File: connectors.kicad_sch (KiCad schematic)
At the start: 1 part, among them J1 Header_to_RPi

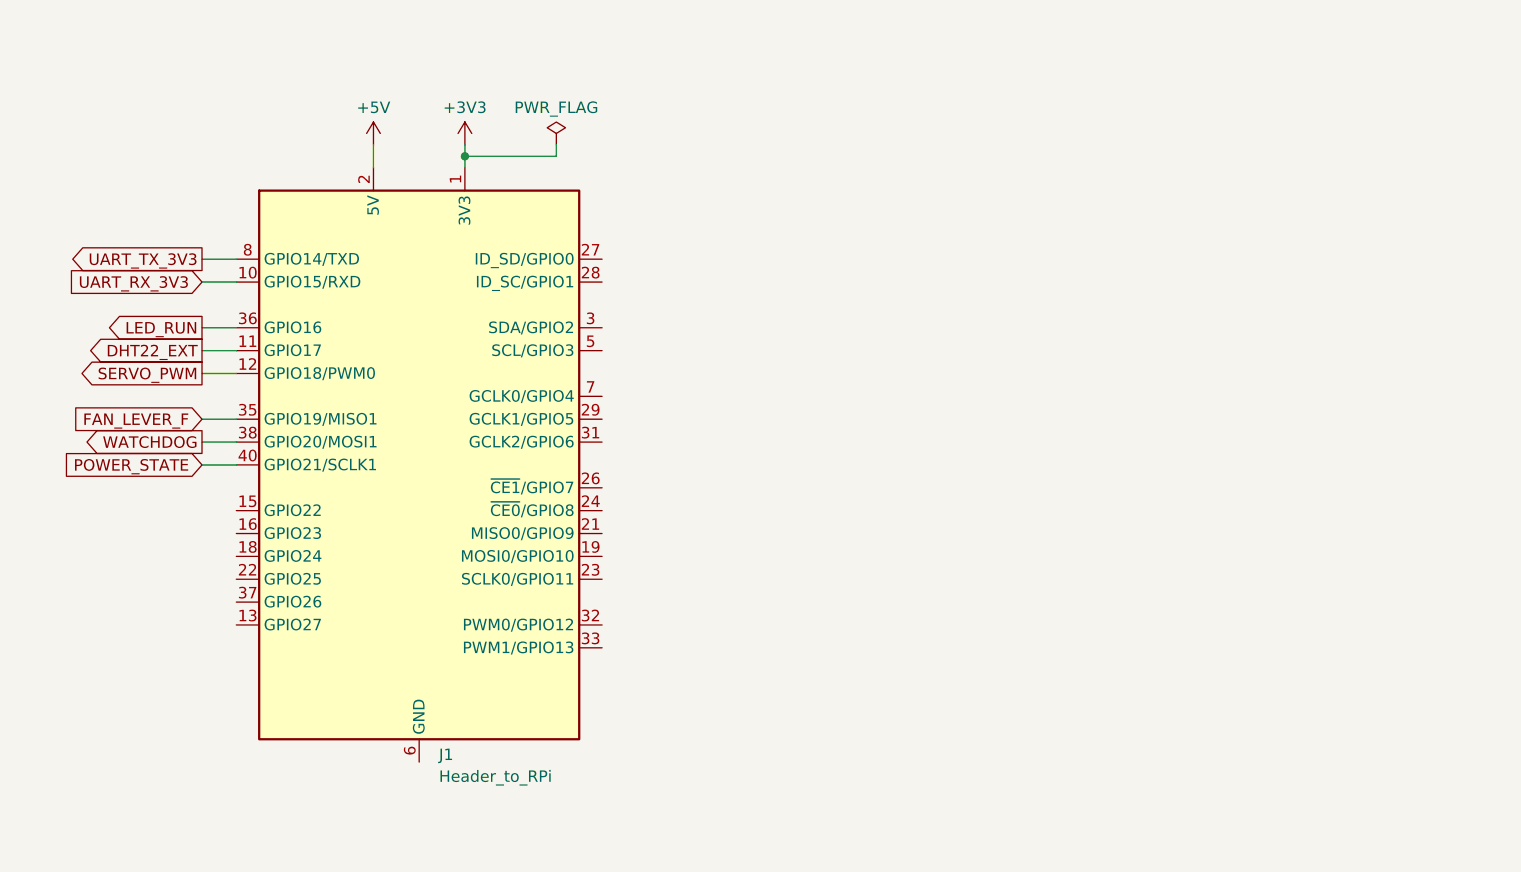
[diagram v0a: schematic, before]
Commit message: Connectors for RPi and front panel done (sch)
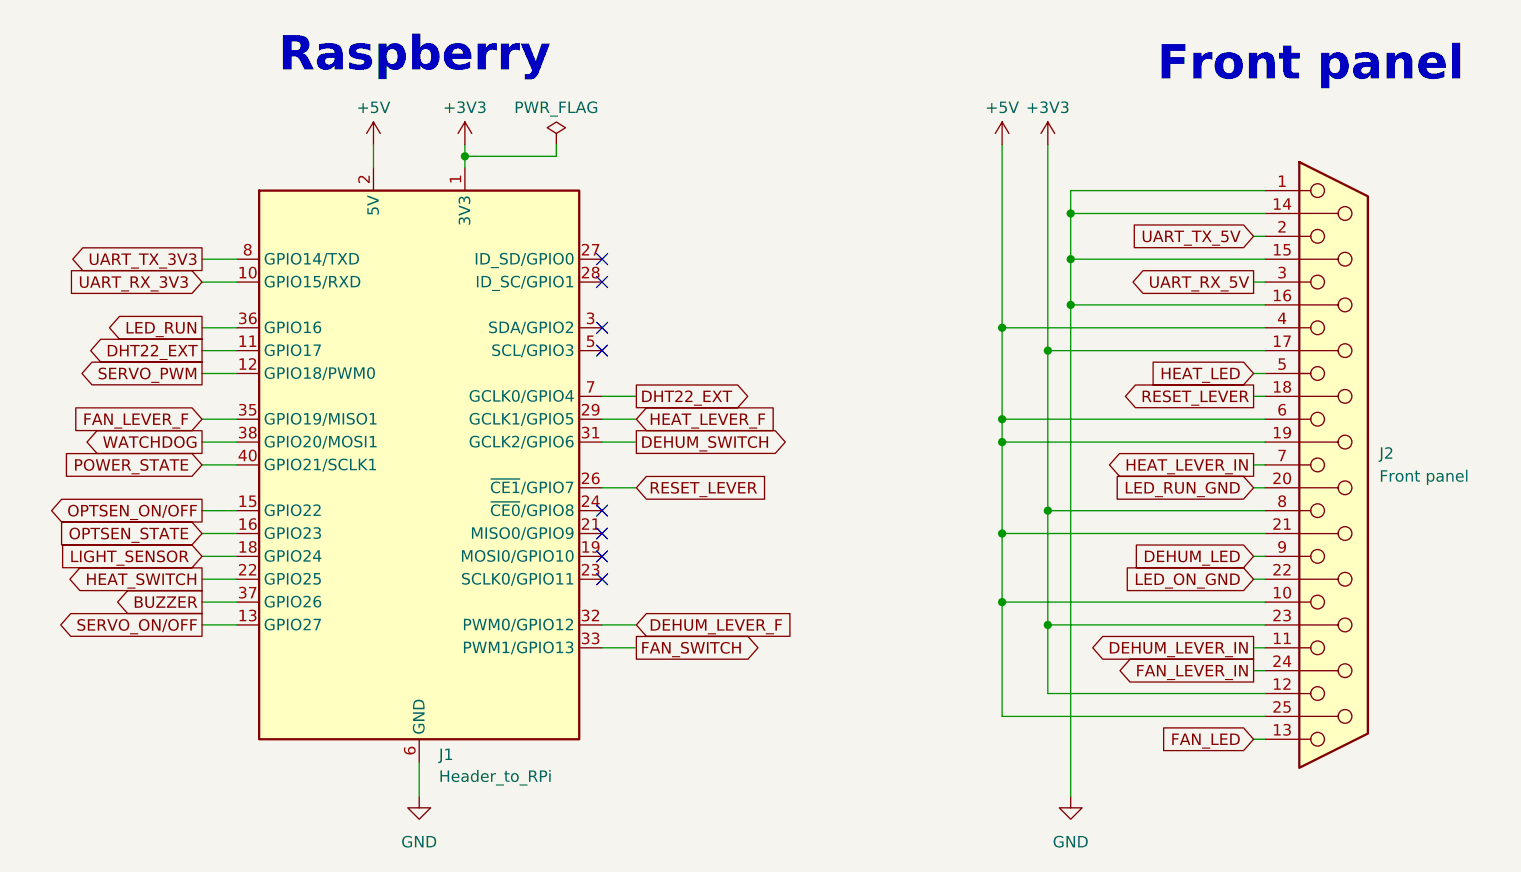
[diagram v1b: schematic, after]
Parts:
- added J2: Front panel, symbol Connector:DB25_Receptacle
- J1: footprint (none) -> Connector_PinHeader_2.54mm:PinHeader_2x20_P2.54mm_Vertical
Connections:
- net +3V3: now also J2.12, J2.17 (P17), J2.23 (P23), J2.8
- net +5V: now also J2.10, J2.19 (P19), J2.21 (P21), J2.25 (P25), J2.4, J2.6
- net DHT22_EXT: now also J1.7 (GCLK0/GPIO4)
- net SERVO_ON/OFF: now reaches J1.13 (GPIO27)
- net GND: now reaches J1.14 (GND), J1.20 (GND), J1.25 (GND), J1.30 (GND), J1.34 (GND), J1.39 (GND), J1.6 (GND), J1.9 (GND)
- net GND: now also J2.1, J2.14 (P14), J2.15 (P15), J2.16 (P16)
- net OPTSEN_ON/OFF: now reaches J1.15 (GPIO22)
- net OPTSEN_STATE: now reaches J1.16 (GPIO23)
- net LIGHT_SENSOR: now reaches J1.18 (GPIO24)
- net HEAT_SWITCH: now reaches J1.22 (GPIO25)
- net RESET_LEVER: now reaches J1.26 (~{CE1}/GPIO7)
- net RESET_LEVER: now also J2.18 (P18)
- net HEAT_LEVER_F: now reaches J1.29 (GCLK1/GPIO5)
- net DEHUM_SWITCH: now reaches J1.31 (GCLK2/GPIO6)
- net DEHUM_LEVER_F: now reaches J1.32 (PWM0/GPIO12)
- net FAN_SWITCH: now reaches J1.33 (PWM1/GPIO13)
- net BUZZER: now reaches J1.37 (GPIO26)
- new net DEHUM_LED: J2.9
- new net DEHUM_LEVER_IN: J2.11
- new net FAN_LED: J2.13
- new net FAN_LEVER_IN: J2.24 (P24)
- new net HEAT_LED: J2.5
- new net HEAT_LEVER_IN: J2.7
- new net LED_ON_GND: J2.22 (P22)
- new net LED_RUN_GND: J2.20 (P20)
- new net UART_RX_5V: J2.3
- new net UART_TX_5V: J2.2
- no-connect marks 0 -> 8
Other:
- note added: "Front panel"
- note added: "Raspberry"

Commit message: Connectors done, WIP on power
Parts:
- added J10: DHT INT, symbol Connector:Conn_01x03_Pin
- added J11: DHT EXT, symbol Connector:Conn_01x03_Pin
- added J3: DEHUM, symbol Connector:Conn_01x02_Pin
- added J4: HEAT, symbol Connector:Conn_01x02_Pin
- added J5: FAN, symbol Connector:Conn_01x02_Pin
- added J6: BUZZER, symbol Connector:Conn_01x02_Pin
- added J7: LIGHTSENSOR, symbol Connector:Conn_01x02_Pin
- added J8: SERVO, symbol Connector:Conn_01x03_Pin
- added J9: POWER_IN, symbol Connector:Conn_01x02_Pin
- added R1, R2: 4.7k, symbol Device:R
- J2: footprint (none) -> Connector_Dsub:DSUB-25_Female_Vertical_P2.77x2.84mm
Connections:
- net +3V3: now also J10.3 (Pin_3), J11.3 (Pin_3), J7.1 (Pin_1), R1.2, R2.2
- net +5V: now also J8.3 (Pin_3)
- net DHT22_EXT: now also J11.2 (Pin_2), R2.1
- net GND: now also J10.1 (Pin_1), J11.1 (Pin_1), J9.1 (Pin_1)
- net SERVO_PWM: now also J8.2 (Pin_2)
- new net +12V: J6.2 (Pin_2)
- new net BUZZER_GND: J6.1 (Pin_1)
- new net DEHUM_RELAY_+: J3.2 (Pin_2)
- new net DEHUM_RELAY_GND: J3.1 (Pin_1)
- new net DHT22_INT: J10.2 (Pin_2), R1.1
- new net FAN_RELAY_+: J5.2 (Pin_2)
- new net FAN_RELAY_GND: J5.1 (Pin_1)
- new net HEAT_RELAY_+: J4.2 (Pin_2)
- new net HEAT_RELAY_GND: J4.1 (Pin_1)
- new net LIGHTSEN_SIG: J7.2 (Pin_2)
- new net POWER+: J9.2 (Pin_2)
- new net SERVO_GND: J8.1 (Pin_1)
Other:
- note added: "Buzzer"
- note added: "DHT EXT"
- note added: "DHT INT"
- note added: "Dehum"
- note added: "Fan"
- note added: "Heat"
- note added: "Light sensor"
- note added: "Power IN"
- note added: "Servo"

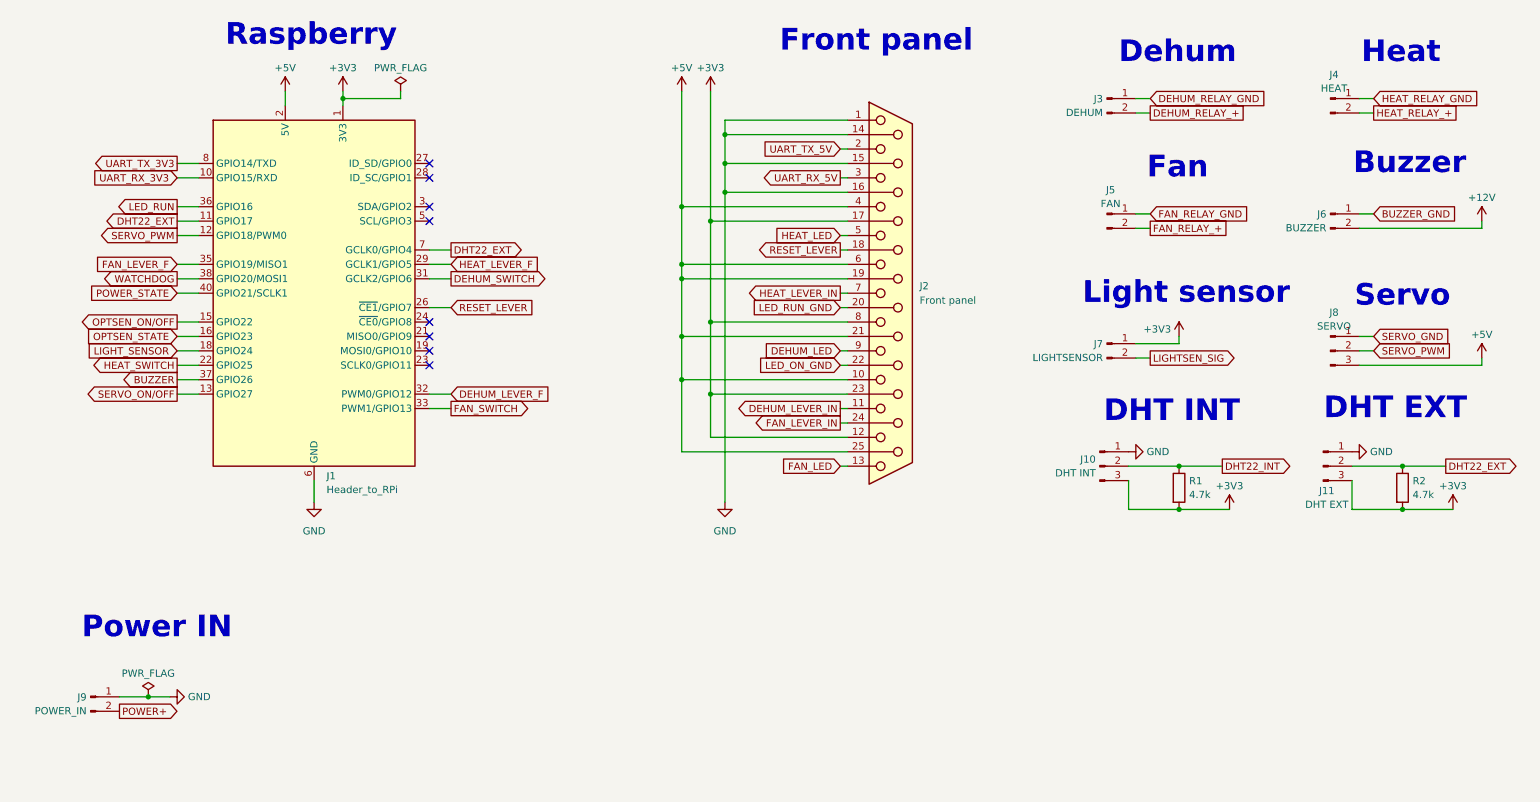
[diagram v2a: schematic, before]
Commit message: Added power surge protection
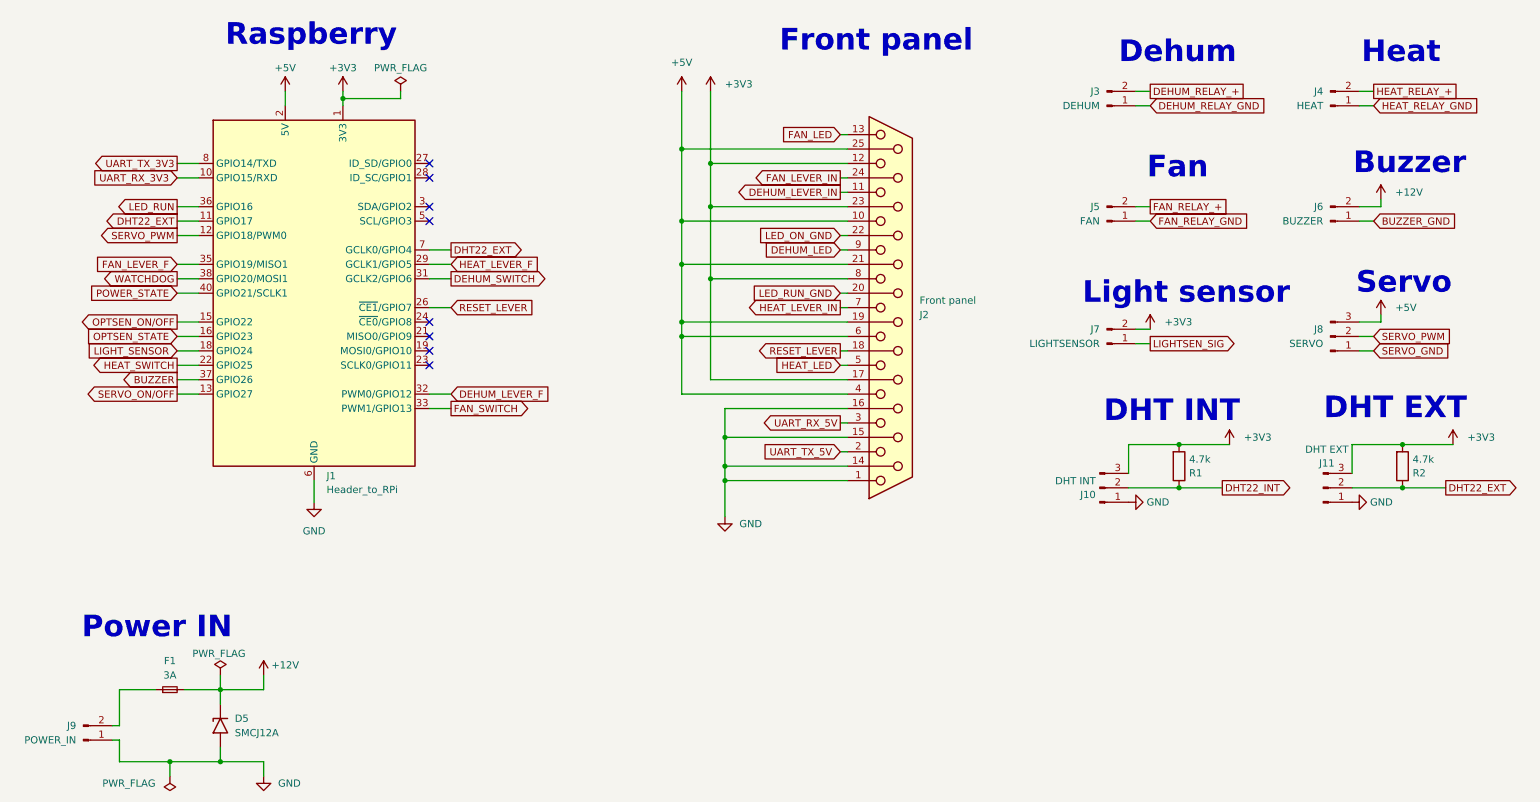
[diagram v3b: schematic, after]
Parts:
- added D5: SMCJ12A, Diode_SMD:D_SMA, symbol Diode:SMAJ12A
- added F1: 3A, symbol Device:Fuse_Small
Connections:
- net +12V: now also D5.1 (A1), F1.2
- net +3V3: now also J7.2 (Pin_2); no longer J7.1 (Pin_1)
- net GND: now also D5.2 (A2)
- net LIGHTSEN_SIG: now also J7.1 (Pin_1); no longer J7.2 (Pin_2)
- net POWER+: no longer names the net of J9.2 (Pin_2)
- net POWER+: now also F1.1
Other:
- moved on the sheet: J10, J11, J2, J3, J4, J5, J6, J7, J8, J9, R1, R2

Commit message: Schematic done (for now), WIP on layout
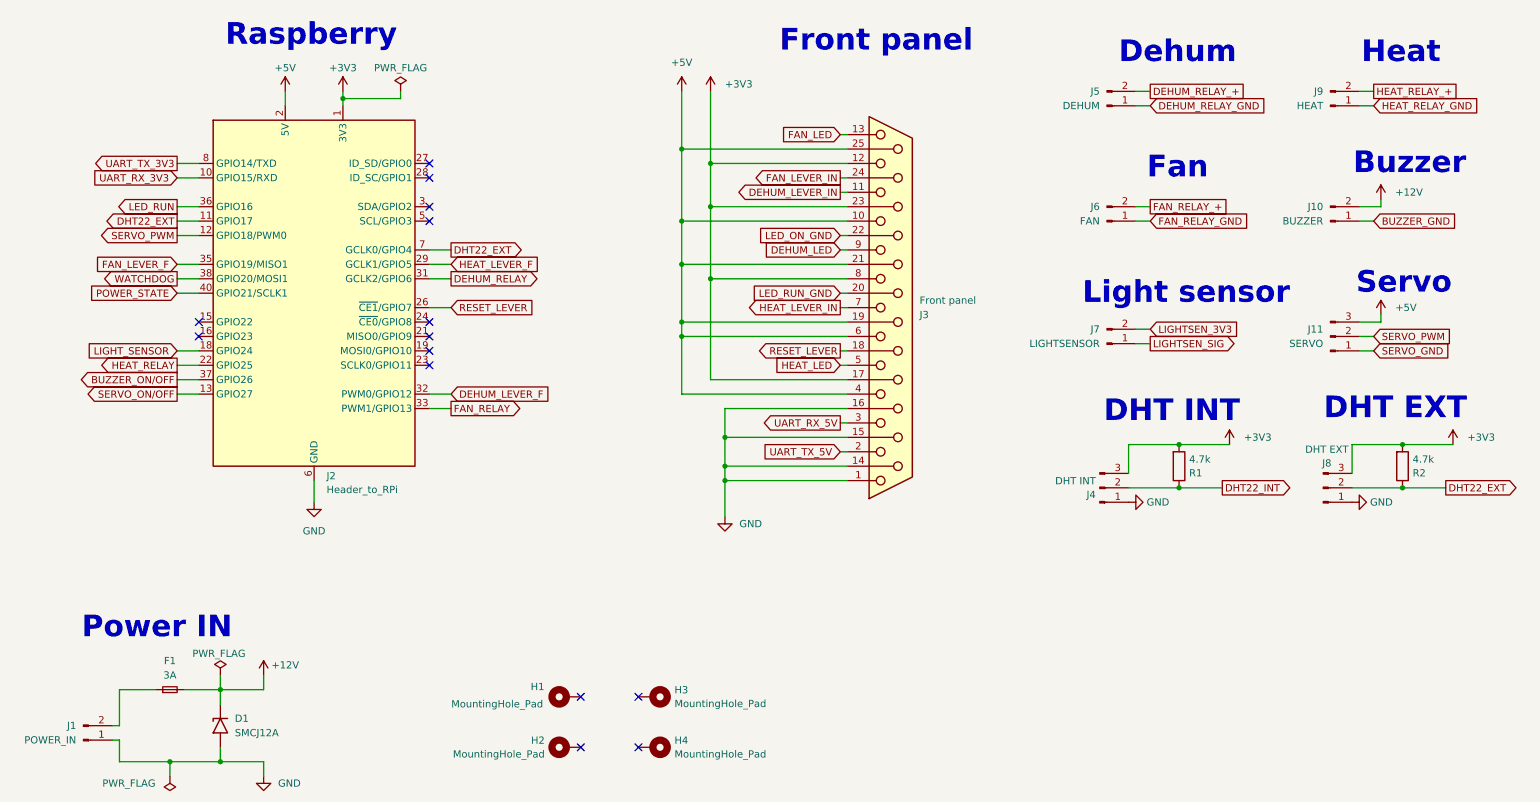
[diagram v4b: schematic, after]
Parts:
- added H1, H2, H3, H4: MountingHole_Pad, MountingHole:MountingHole_2.2mm_M2_ISO14580_Pad_TopBottom, symbol Mechanical:MountingHole_Pad
- D1: renamed from D5; footprint Diode_SMD:D_SMA -> Diode_SMD:D_SMC_Handsoldering
- F1: footprint (none) -> Fuse:Fuseholder_Littelfuse_Nano2_154x
- J1: renamed from J9; footprint (none) -> Connector_JST:JST_XH_B2B-XH-A_1x02_P2.50mm_Vertical
- J10: renamed from J6; footprint (none) -> Connector_JST:JST_XH_B2B-XH-A_1x02_P2.50mm_Vertical
- J11: renamed from J8; footprint (none) -> Connector_JST:JST_XH_B3B-XH-A_1x03_P2.50mm_Vertical
- J4: renamed from J10; footprint (none) -> Connector_JST:JST_XH_B3B-XH-A_1x03_P2.50mm_Vertical
- J5: renamed from J3; footprint (none) -> Connector_JST:JST_XH_B2B-XH-A_1x02_P2.50mm_Vertical
- J6: renamed from J5; footprint (none) -> Connector_JST:JST_XH_B2B-XH-A_1x02_P2.50mm_Vertical
- J7: footprint (none) -> Connector_JST:JST_XH_B2B-XH-A_1x02_P2.50mm_Vertical
- J8: renamed from J11; footprint (none) -> Connector_JST:JST_XH_B3B-XH-A_1x03_P2.50mm_Vertical
- J9: renamed from J4; footprint (none) -> Connector_JST:JST_XH_B2B-XH-A_1x02_P2.50mm_Vertical
- R1, R2: footprint (none) -> Resistor_SMD:R_0603_1608Metric_Pad0.98x0.95mm_HandSolder
- renumbered J1 to J2, J2 to J3
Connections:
- net +3V3: no longer J7.2 (Pin_2)
- net BUZZER renamed BUZZER_ON/OFF
- net DEHUM_SWITCH renamed DEHUM_RELAY
- net FAN_SWITCH renamed FAN_RELAY
- net HEAT_SWITCH renamed HEAT_RELAY
- net OPTSEN_ON/OFF: no longer names the net of J2.15 (GPIO22)
- net OPTSEN_STATE: no longer names the net of J2.16 (GPIO23)
- new net LIGHTSEN_3V3: J7.2 (Pin_2)
- no-connect marks 8 -> 14
